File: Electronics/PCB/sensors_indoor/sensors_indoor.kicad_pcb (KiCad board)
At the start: 2 copper layers, 50 x 50 mm, 10 parts, among them J1 B5B-ZR, U1 SHT45-AD1F, U2 LPS22DF, U3 SCD41-D-R2, U4 TSOP38436, U5 STM32WBA5MMG, U6 SGP41, U7 SPS30

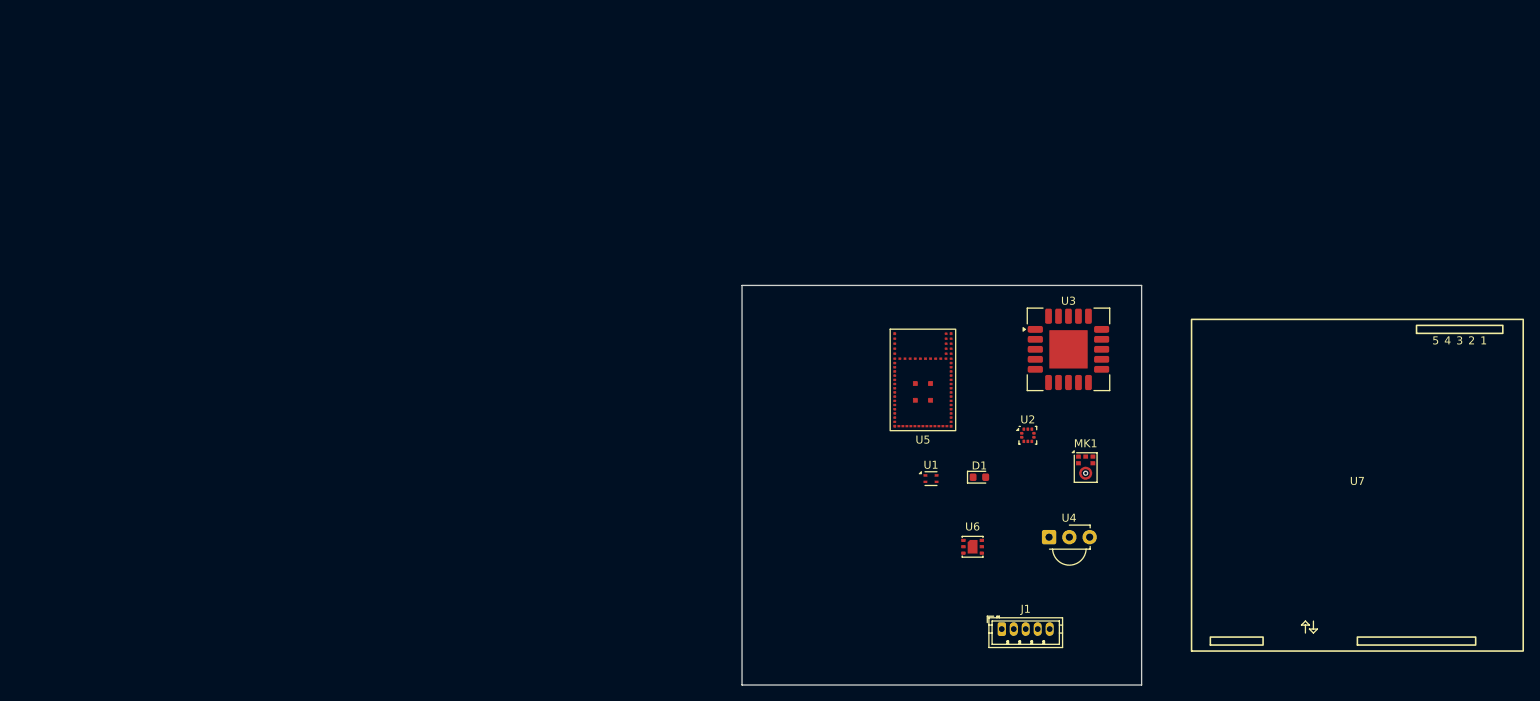
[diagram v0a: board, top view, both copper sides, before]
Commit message: Arranged sensors on PCB, added MRAM and USB-C socket
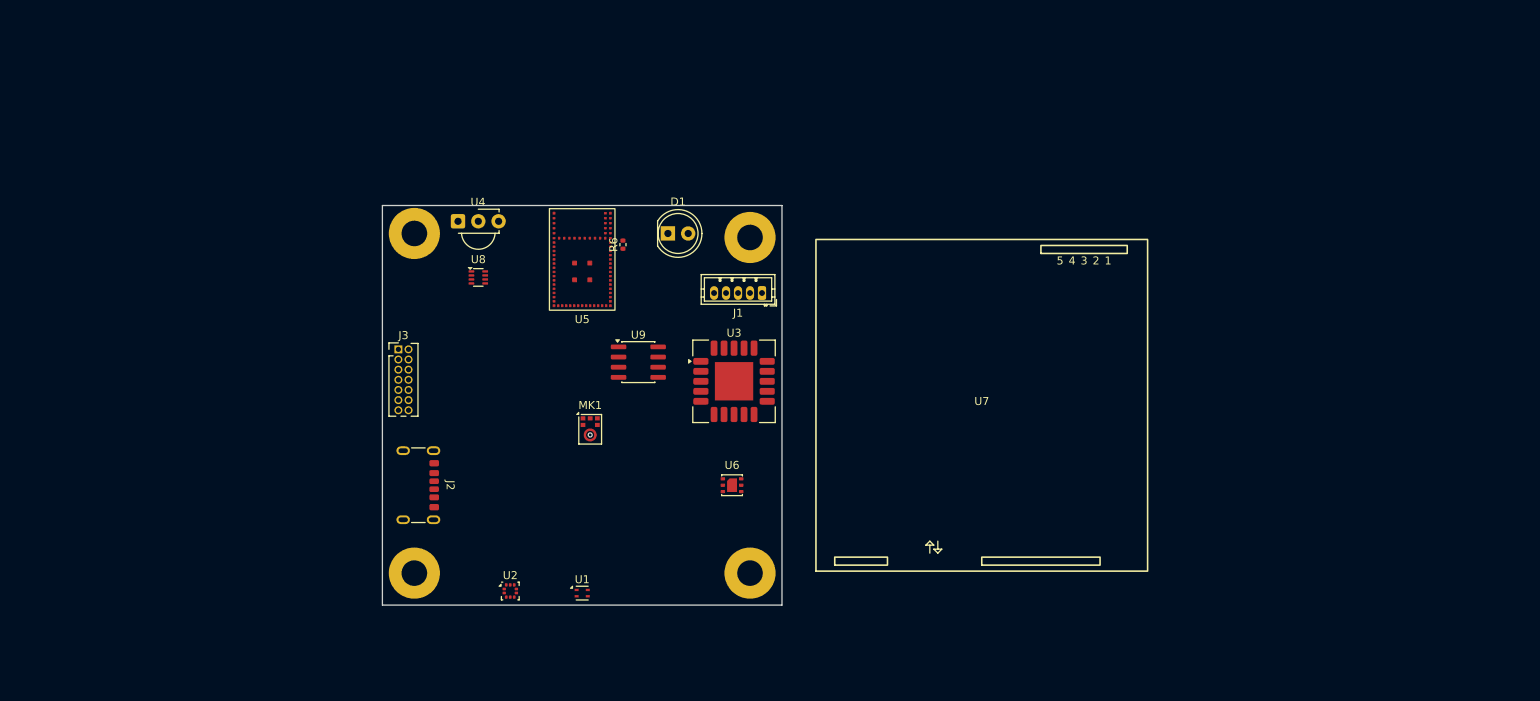
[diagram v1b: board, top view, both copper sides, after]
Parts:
- added J2: USB4125-GF-A, Connector_USB:USB_C_Receptacle_GCT_USB4125-xx-x-0190_6P_TopMnt_Horizontal, F.Cu at (78.4, 110.0)
- added J3: Conn_ST_STDC14, Connector_PinHeader_1.27mm:PinHeader_2x07_P1.27mm_Vertical, F.Cu at (77.0, 93.0)
- added R6: 0R, Resistor_SMD:R_0402_1005Metric, F.Cu at (105.1, 79.9)
- added REF**: MountingHole_3.2mm_M3_Pad, MountingHole:MountingHole_3.2mm_M3_Pad, F.Cu at (79.0, 78.5)
- added REF**: MountingHole_3.2mm_M3_Pad, MountingHole:MountingHole_3.2mm_M3_Pad, F.Cu at (121.0, 79.0)
- added REF**: MountingHole_3.2mm_M3_Pad, MountingHole:MountingHole_3.2mm_M3_Pad, F.Cu at (79.0, 121.0)
- added REF**: MountingHole_3.2mm_M3_Pad, MountingHole:MountingHole_3.2mm_M3_Pad, F.Cu at (121.0, 121.0)
- added U8: OPT4001DTSR, DWlib:TI_SOT-5X3_OPT4001DTSR, F.Cu at (87.0, 84.0)
- added U9: FM24CL16B, Package_SO:SOIC-8_3.9x4.9mm_P1.27mm, F.Cu at (107.0, 94.6)
- D1: footprint LED_SMD:LED_0603_1608Metric -> LED_THT:LED_D5.0mm_Clear
- moved U4 83.9 mm to (84.5, 77.0)
- moved U2 67.6 mm to (91.0, 123.2)
- moved MK1 62.2 mm to (101.0, 103.0)
- moved J1 51.7 mm to (122.5, 86.0), turned to 180 degrees
- moved D1 49.5 mm to (110.7, 78.5)
- moved U7 48.1 mm to (150.0, 100.0)
- moved U1 45.9 mm to (100.0, 123.5)
- moved U5 45.2 mm to (100.0, 81.8)
- moved U3 42.0 mm to (119.0, 97.0)
- moved U6 31.1 mm to (118.8, 110.0)
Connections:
- J1 pad 2: unconnected-(J1-Pin_2-Pad2) -> /UART_MOSI
- J1 pad 3: unconnected-(J1-Pin_3-Pad3) -> /UART_MISO
- J1 pad 5: unconnected-(J1-Pin_5-Pad5) -> GND
- MK1 pad 1: unconnected-(MK1-WS-Pad1) -> /I2S_FS
- MK1 pad 3: unconnected-(MK1-GND-Pad3) -> GND
- MK1 pad 4: unconnected-(MK1-SCK-Pad4) -> /I2S_SCK
- MK1 pad 6: unconnected-(MK1-SD-Pad6) -> /I2S_SD
- U1 pad 1: unconnected-(U1-SDA-Pad1) -> /I2C1_SDA
- U1 pad 2: unconnected-(U1-SCL-Pad2) -> /I2C1_SCL
- U1 pad 3: unconnected-(U1-VDD-Pad3) -> Net-(U1-VDD)
- U1 pad 4: unconnected-(U1-VSS-Pad4) -> GND
- U2 pad 2: unconnected-(U2-SCL-Pad2) -> /SPI_SCLK
- U2 pad 3: Net-(U2-GND-Pad3) -> GND
- U2 pad 4: unconnected-(U2-SDA-Pad4) -> /SPI_MOSI
- U2 pad 5: unconnected-(U2-SA0-Pad5) -> /SPI_MISO
- U2 pad 6: unconnected-(U2-~{CS}-Pad6) -> /SPI_CS
- U2 pad 7: unconnected-(U2-INT_DRDY-Pad7) -> /INT_PRES
- U2 pad 8: unconnected-(U2-GND_IO-Pad8) -> GND
- U2 pad 9: Net-(U2-GND-Pad3) -> GND
- U3 pad 10: unconnected-(U3-SDA-Pad10) -> /I2C_SCL
- U3 pad 20: Net-(U3-GND-Pad20) -> GND
- U3 pad 21: Net-(U3-GND-Pad20) -> GND
- U3 pad 6: Net-(U3-GND-Pad20) -> GND
- U3 pad 9: unconnected-(U3-SCL-Pad9) -> /I2C_SDA
- U4 pad 1: unconnected-(U4-OUT-Pad1) -> /IR_IN
- U4 pad 2: unconnected-(U4-GND-Pad2) -> GND
- U5 pad 14: unconnected-(U5-PA7-Pad14) -> /I2C3_SDA
- U5 pad 15: unconnected-(U5-PA6-Pad15) -> /I2C3_SCL
- U5 pad 18: unconnected-(U5-PA0-Pad18) -> /SPI_SCLK
- U5 pad 20: unconnected-(U5-VDDA-Pad20) -> /VDD_MCU
- U5 pad 22: unconnected-(U5-VDD-Pad22) -> /VDD_MCU
- U5 pad 26: unconnected-(U5-PB9-Pad26) -> /SPI_MISO
- U5 pad 27: unconnected-(U5-PA5-Pad27) -> /SPI_CS
- U5 pad 29: unconnected-(U5-PB8-Pad29) -> /SPI_MOSI
- U5 pad 30: unconnected-(U5-PB6-Pad30) -> /I2S_SCK
- U5 pad 31: unconnected-(U5-PB7-Pad31) -> /I2S_SD
- U5 pad 32: unconnected-(U5-PB3-Pad32) -> /SWO
- U5 pad 33: unconnected-(U5-PB5-Pad33) -> /I2S_FS
- U5 pad 37: unconnected-(U5-PA14-Pad37) -> /SWCLK
- U5 pad 38: unconnected-(U5-PA13-Pad38) -> /SWDIO
- U5 pad 39: unconnected-(U5-PA12-Pad39) -> /VCP_TX
- U5 pad 40: unconnected-(U5-PA11-Pad40) -> /VCP_RX
- U5 pad 41: unconnected-(U5-PB2-Pad41) -> /I2C1_SCL
- U5 pad 42: unconnected-(U5-PB1-Pad42) -> /I2C1_SDA
- U5 pad 46: unconnected-(U5-BOOT0-Pad46) -> /BOOT0
- U5 pad 48: unconnected-(U5-~{NRST}-Pad48) -> /NRST
- U5 pad 50: unconnected-(U5-ANT_OUT-Pad50) -> /ANT
- U5 pad 51: unconnected-(U5-ANT_IN-Pad51) -> Net-(U5-ANT_IN)
- U6 pad 2: unconnected-(U6-VSS-Pad2) -> GND
- U6 pad 3: unconnected-(U6-SDA-Pad3) -> /I2C_SDA
- U6 pad 6: unconnected-(U6-SCL-Pad6) -> /I2C_SCL
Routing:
- added copper zone on In1.Cu, net GND
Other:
- copper layers 2 -> 4
- rule pad_to_mask_clearance: 0 -> 0.05

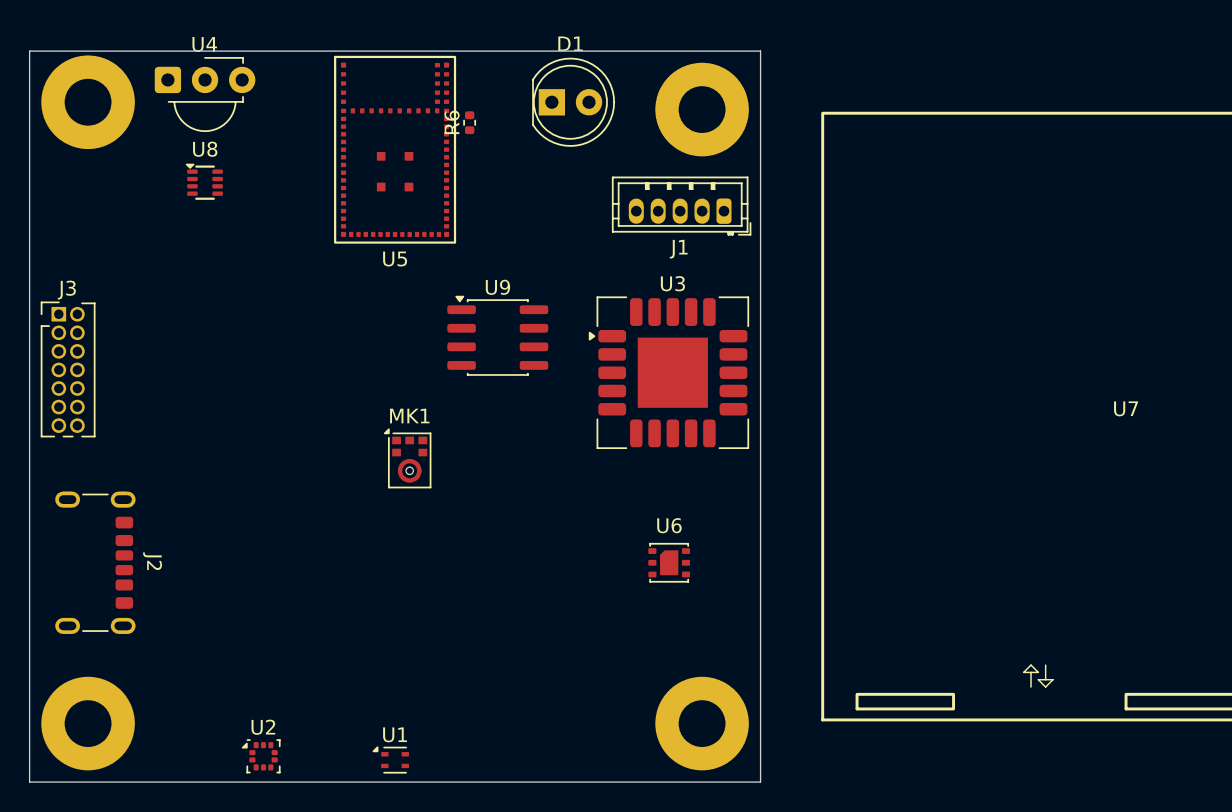
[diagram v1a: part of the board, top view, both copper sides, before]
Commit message: Split schematic into 3 for clarity
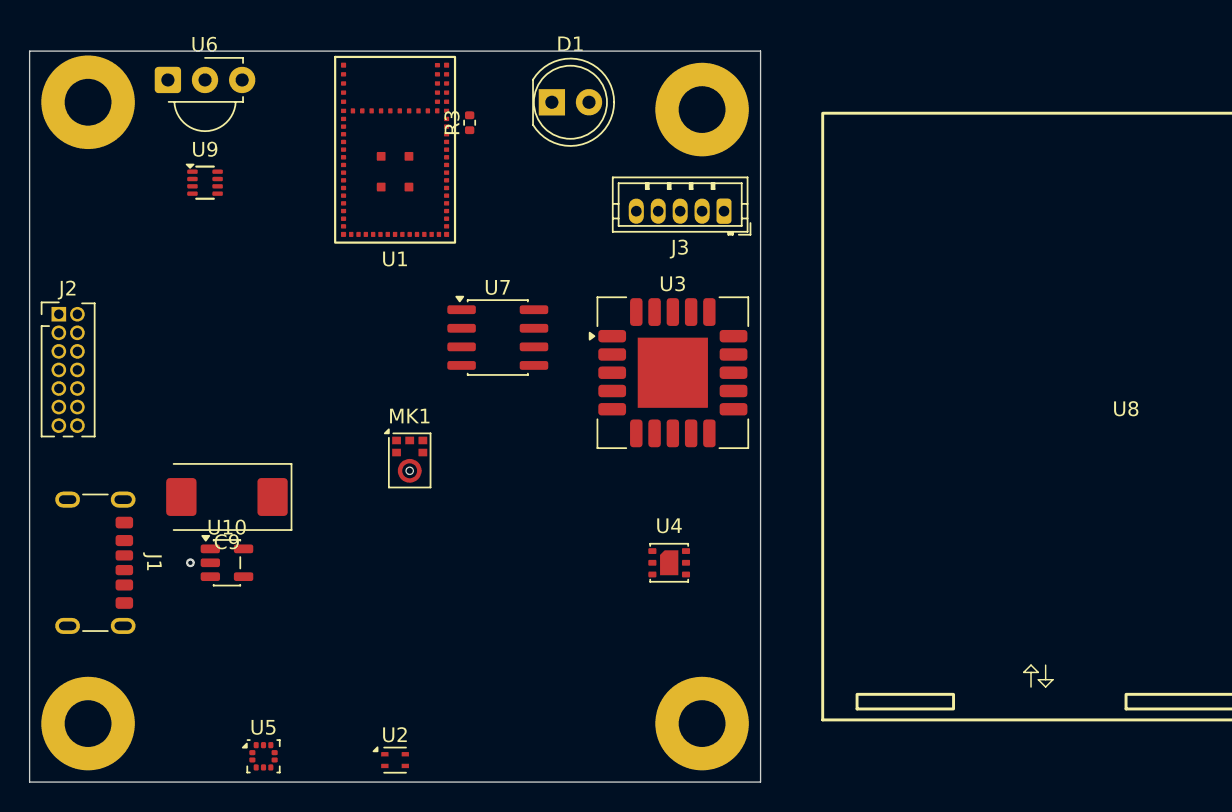
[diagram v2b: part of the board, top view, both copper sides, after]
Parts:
- added C9: 47u, Capacitor_Tantalum_SMD:CP_EIA-7343-31_Kemet-D, F.Cu at (88.5, 105.5)
- added U10: MIC5219-3.3YM5, Package_TO_SOT_SMD:SOT-23-5, F.Cu at (88.5, 110.0)
- renumbered J2 to J1, J3 to J2, J1 to J3, R6 to R3, U5 to U1, U1 to U2, U6 to U4, U2 to U5, U4 to U6, U9 to U7, U7 to U8, U8 to U9
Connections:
- net /ANT renamed /indoor_MCU/ANT
- net /BOOT0 renamed /indoor_MCU/BOOT0
- net /I2C1_SCL renamed I2C1_SCL
- net /I2C1_SDA renamed I2C1_SDA
- net /I2C3_SCL renamed I2C3_SCL
- net /I2C3_SDA renamed I2C3_SDA
- net /INT_ALS renamed INT_ALS
- net /INT_PRES renamed INT_PRES
- net /IR_IN renamed IR_IN
- net /NRST renamed /indoor_MCU/NRST
- net /SWCLK renamed /indoor_MCU/SWCLK
- net /SWDIO renamed /indoor_MCU/SWDIO
- net /SWO renamed /indoor_MCU/SWO
- net /VCP_RX renamed /indoor_MCU/VCP_RX
- net /VCP_TX renamed /indoor_MCU/VCP_TX
- net /VDD_MCU renamed /indoor_MCU/VDD_MCU
- J3 pad 2: /UART_MOSI -> unconnected-(J3-Pin_2-Pad2)
- J3 pad 3: /UART_MISO -> unconnected-(J3-Pin_3-Pad3)
- MK1 pad 1: /I2S_FS -> /indoor_sensors/I2S_FS
- MK1 pad 4: /I2S_SCK -> /indoor_sensors/I2S_SCK
- MK1 pad 6: /I2S_SD -> /indoor_sensors/I2S_SD
- U1 pad 18: /SPI_SCLK -> /indoor_MCU/SPI_SCLK
- U1 pad 26: /SPI_MISO -> /indoor_MCU/SPI_MISO
- U1 pad 27: /SPI_CS -> /indoor_MCU/SPI_CS
- U1 pad 29: /SPI_MOSI -> /indoor_MCU/SPI_MOSI
- U1 pad 30: /I2S_SCK -> /indoor_MCU/I2S_SCK
- U1 pad 31: /I2S_SD -> /indoor_MCU/I2S_SD
- U1 pad 33: /I2S_FS -> /indoor_MCU/I2S_FS
- U3 pad 10: /I2C_SCL -> unconnected-(U3-SDA-Pad10)
- U3 pad 9: /I2C_SDA -> unconnected-(U3-SCL-Pad9)
- U4 pad 3: /I2C_SDA -> unconnected-(U4-SDA-Pad3)
- U4 pad 6: /I2C_SCL -> unconnected-(U4-SCL-Pad6)
- U5 pad 2: /SPI_SCLK -> /indoor_sensors/SPI_SCLK
- U5 pad 4: /SPI_MOSI -> /indoor_sensors/SPI_MOSI
- U5 pad 5: /SPI_MISO -> /indoor_sensors/SPI_MISO
- U5 pad 6: /SPI_CS -> /indoor_sensors/SPI_CS
- U9 pad 5: /I2C_SCL -> unconnected-(U9-SCL-Pad5)
- U9 pad 8: /I2C_SDA -> unconnected-(U9-SDA-Pad8)
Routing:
- net (no net): vias 0 -> 1
